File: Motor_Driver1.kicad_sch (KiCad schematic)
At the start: 20 parts, among them J801 Conn_01x02_Socket, U801 DMHT6016LFJ-13, U802 DRV8701

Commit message: all layouts re-designed.Next step routing...
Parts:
- C804: footprint Capacitor_SMD:C_Elec_8x10.2 -> Capacitor_SMD:CP_Elec_8x10
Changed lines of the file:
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@@
 			)
 		)
-		(property "Footprint" "Capacitor_SMD:C_Elec_8x10.2"
+		(property "Footprint" "Capacitor_SMD:CP_Elec_8x10"
 			(at 156.0904 86.4384 0)
 			(effects

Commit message: motor driver nsleep pin pull-up resistor connected 12V plane by 3.3V voltage divider.
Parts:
- added R812: 3k3, Resistor_SMD:R_0805_2012Metric, symbol Device:R_Small
- R811: value 10k -> 7k2
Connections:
- net +3V3 is gone; now on an unnamed net: R811.1
- net +12V: now also R811.2
- net GND: now also R812.2
- net at U802.13 (nSLEEP): now also R812.1; no longer R811.2

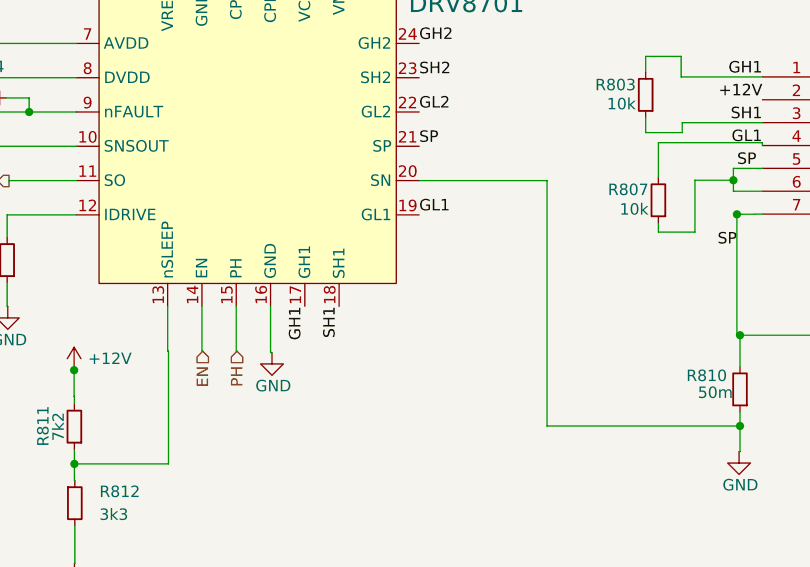
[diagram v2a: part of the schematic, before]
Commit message: 1.8V voltage regülator block placed in top side to provide a solid return path
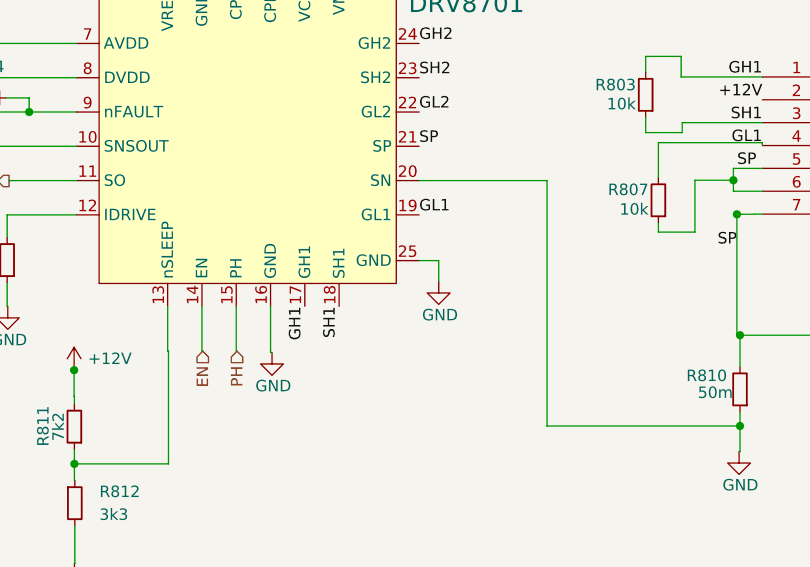
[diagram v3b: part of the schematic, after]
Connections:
- net GND: now also U802.25 (GND)
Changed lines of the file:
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@@
 	(wire
 		(pts
+			(xy 132.049 129.8619) (xy 134.2231 129.8619)
+		)
+		(stroke
+			(width 0)
+			(type default)
+		)
+	)
+	(wire
+		(pts
 			(xy 158.6339 126.6956) (xy 162.6944 126.6956)
 		)
@@
 	(wire
 		(pts
+			(xy 134.2231 129.8619) (xy 134.2231 132.1891)
+		)
+		(stroke
+			(width 0)
+			(type default)
+		)
+	)
+	(wire
+		(pts
 			(xy 143.3675 74.7098) (xy 143.3675 81.6836)
 		)
@@
 	(symbol
 		(lib_id "power:GND")
+		(at 134.2231 132.1891 0)
+		(unit 1)
+		(exclude_from_sim no)
+		(in_bom yes)
+		(on_board yes)
+		(dnp no)
+		(property "Reference" "#PWR0811"
+			(at 134.2231 138.5391 0)
+			(effects
+				(font
+					(size 1.27 1.27)
+				)
+				(hide yes)
+			)
+		)
+		(property "Value" "GND"
+			(at 134.3701 135.9135 0)
+			(effects
+				(font
+					(size 1.27 1.27)
+				)
+			)
+		)
+		(property "Footprint" ""
+			(at 134.2231 132.1891 0)
+			(effects
+				(font
+					(size 1.27 1.27)
+				)
+				(hide yes)
+			)
+		)
+		(property "Datasheet" ""
+			(at 134.2231 132.1891 0)
+			(effects
+				(font
+					(size 1.27 1.27)
+				)
+				(hide yes)
+			)
+		)
+		(property "Description" "Power symbol creates a global label with name \"GND\" , ground"
+			(at 134.2231 132.1891 0)
+			(effects
+				(font
+					(size 1.27 1.27)
+				)
+				(hide yes)
+			)
+		)
+		(pin "1"
+		)
+		(instances
+			(project "mixed signal board project"
+				(path "/8a424437-6f3e-424c-a786-3b8b285eee60/e71aabe1-ea26-4cd5-b208-bfd96f8b8470"
+					(reference "#PWR0811")
+					(unit 1)
+				)
+			)
+		)
+	)
+	(symbol
+		(lib_id "power:GND")
 		(at 167.6005 151.0858 0)
 		(unit 1)
@@
 		(pin "5"
 		)
+		(pin "25"
+		)
 		(instances

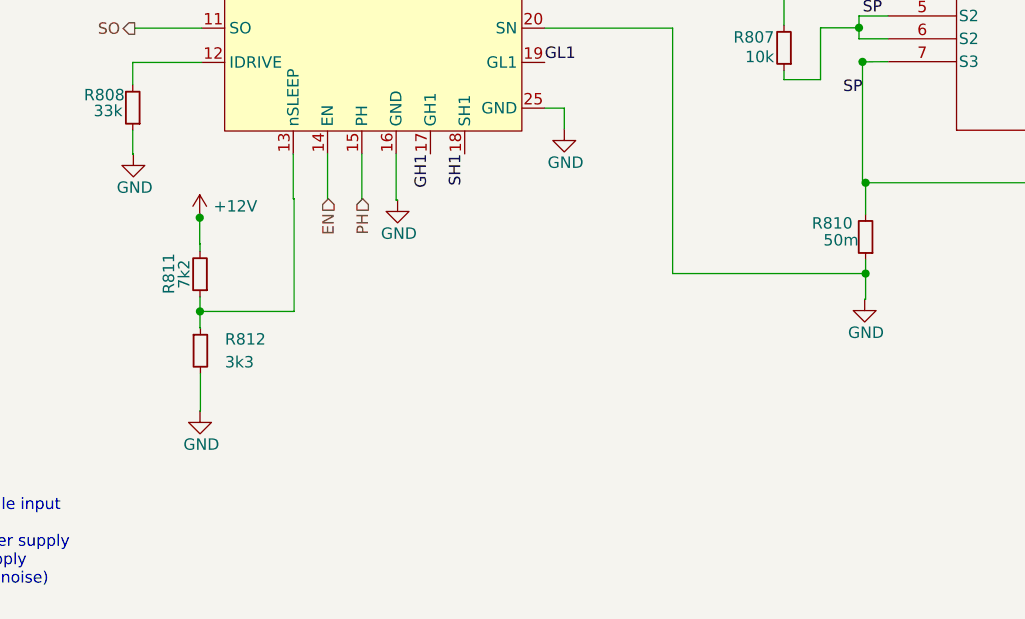
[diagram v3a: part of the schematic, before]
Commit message: some design failures reviewed(MIC VDD is 1V8, Motor Drivers' pull-up to DVDD pin, I2C net fixed). Routing mostly done.
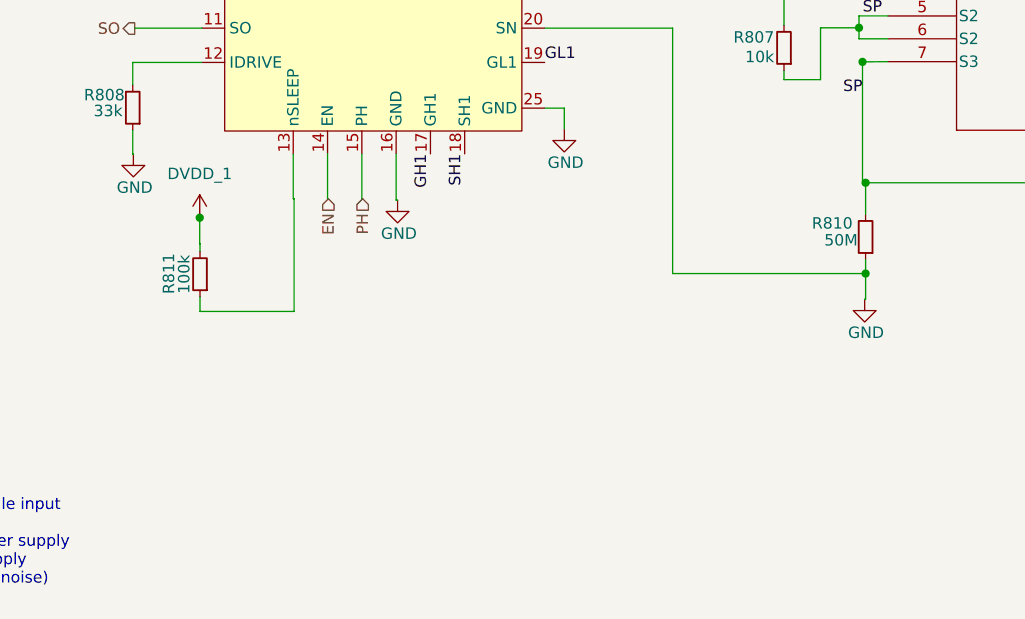
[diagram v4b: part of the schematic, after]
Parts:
- removed R812: 3k3, Resistor_SMD:R_0805_2012Metric, symbol Device:R_Small
- R810: value 50m -> 50M
- R811: value 7k2 -> 100k
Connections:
- net +12V: no longer R811.2
- net DVDD_1: now also R811.2
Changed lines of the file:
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@@
 	)
 	(junction
-		(at 93.7448 152.4504)
-		(diameter 0)
-		(color 0 0 0 0)
-	)
-	(junction
 		(at 143.3675 81.6836)
 		(diameter 0)
@@
 	(wire
 		(pts
-			(xy 93.7448 154.2757) (xy 93.7936 154.2757)
-		)
-		(stroke
-			(width 0)
-			(type default)
-		)
-	)
-	(wire
-		(pts
 			(xy 59.5287 90.65) (xy 59.5287 92.5553)
 		)
@@
 	(wire
 		(pts
-			(xy 93.7448 152.4504) (xy 93.7448 154.2757)
-		)
-		(stroke
-			(width 0)
-			(type default)
-		)
-	)
-	(wire
-		(pts
 			(xy 119.3681 80.3101) (xy 119.3681 79.006)
 		)
@@
 	(wire
 		(pts
-			(xy 93.7936 159.3557) (xy 93.7936 163.5111)
-		)
-		(stroke
-			(width 0)
-			(type default)
-		)
-	)
-	(wire
-		(pts
 			(xy 123.159 96.8419) (xy 123.159 92.2436)
 		)
@@
 	(wire
 		(pts
-			(xy 93.7936 163.5111) (xy 93.7505 163.5111)
-		)
-		(stroke
-			(width 0)
-			(type default)
-		)
-	)
-	(wire
-		(pts
 			(xy 106.1541 90.55) (xy 106.1541 90.4795)
 		)
@@
 			)
 		)
-		(property "Value" "7k2"
+		(property "Value" "100k"
 			(at 91.9807 148.3146 90)
 			(effects
@@
 			)
 		)
-		(property "Value" "50m"
+		(property "Value" "50M"
 			(at 164.9676 144.5354 0)
 			(effects
@@
 	)
 	(symbol
-		(lib_id "power:GND")
-		(at 93.7505 163.5111 0)
-		(unit 1)
-		(exclude_from_sim no)
-		(in_bom yes)
-		(on_board yes)
-		(dnp no)
-		(property "Reference" "#PWR0418"
-			(at 93.7505 169.8611 0)
-			(effects
-				(font
-					(size 1.27 1.27)
-				)
-				(hide yes)
-			)
-		)
-		(property "Value" "GND"
-			(at 93.8975 167.2355 0)
-			(effects
-				(font
-					(size 1.27 1.27)
-				)
-			)
-		)
-		(property "Footprint" ""
-			(at 93.7505 163.5111 0)
-			(effects
-				(font
-					(size 1.27 1.27)
-				)
-				(hide yes)
-			)
-		)
-		(property "Datasheet" ""
-			(at 93.7505 163.5111 0)
-			(effects
-				(font
-					(size 1.27 1.27)
-				)
-				(hide yes)
-			)
-		)
-		(property "Description" "Power symbol creates a global label with name \"GND\" , ground"
-			(at 93.7505 163.5111 0)
-			(effects
-				(font
-					(size 1.27 1.27)
-				)
-				(hide yes)
-			)
-		)
-		(pin "1"
-		)
-		(instances
-			(project "mixed signal board project"
-				(path "/8a424437-6f3e-424c-a786-3b8b285eee60/e71aabe1-ea26-4cd5-b208-bfd96f8b8470"
-					(reference "#PWR0418")
-					(unit 1)
-				)
-			)
-		)
-	)
-	(symbol
 		(lib_id "power:+3V3")
 		(at 93.7157 142.0364 0)
@@
 			)
 		)
-		(property "Value" "+12V"
-			(at 95.25 140.7663 0)
+		(property "Value" "DVDD_1"
+			(at 93.7157 137.16 0)
 			(effects
 				(font
 					(size 1.27 1.27)
 				)
-				(justify left)
 			)
 		)
@@
 					(unit 1)
 				)
-			)
-		)
-	)
-	(symbol
-		(lib_id "Device:R_Small")
-		(at 93.7936 156.8157 0)
-		(unit 1)
-		(exclude_from_sim no)
-		(in_bom yes)
-		(on_board yes)
-		(dnp no)
-		(fields_autoplaced yes)
-		(property "Reference" "R812"
-			(at 96.52 155.5456 0)
-			(effects
-				(font
-					(size 1.27 1.27)
-				)
-				(justify left)
-			)
-		)
-		(property "Value" "3k3"
-			(at 96.52 158.0856 0)
-			(effects
-				(font
-					(size 1.27 1.27)
-				)
-				(justify left)
-			)
-		)
-		(property "Footprint" "Resistor_SMD:R_0805_2012Metric"
-			(at 93.7936 156.8157 0)
-			(effects
-				(font
-					(size 1.27 1.27)
-				)
-				(hide yes)
-			)
-		)
-		(property "Datasheet" "~"
-			(at 93.7936 156.8157 0)
-			(effects
-				(font
-					(size 1.27 1.27)
-				)
-				(hide yes)
-			)
-		)
-		(property "Description" "Resistor, small symbol"
-			(at 93.7936 156.8157 0)
-			(effects
-				(font
-					(size 1.27 1.27)
-				)
-				(hide yes)
-			)
-		)
-		(pin "2"
-		)
-		(pin "1"
-		)
-		(instances
-			(project ""
-				(path "/8a424437-6f3e-424c-a786-3b8b285eee60/e71aabe1-ea26-4cd5-b208-bfd96f8b8470"
-					(reference "R812")
-					(unit 1)
-				)

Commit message: some additions
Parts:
- renumbered C804 to C?, C805 to C?, C801 to C?, C803 to C?, C806 to C?, C802 to C?, J801 to J?, R811 to R?, R802 to R?, R807 to R?, R803 to R?, R808 to R?, R810 to R?, R806 to R?, R801 to R?, R809 to R?, R805 to R?, R804 to R?, U801 to U?, U802 to U?
